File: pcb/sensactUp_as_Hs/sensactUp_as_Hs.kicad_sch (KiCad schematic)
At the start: 43 parts, among them J1 EXT_ROT, J2 SensactBusConnector, J3 24V+CAN IN, J4 24V+CAN OUT, J5 24V+CAN OUT, J6 24V+CAN OUT, J7 12V LED, Q1 AO3400A, Q2 AO3400A, Q3 AO3400A, SW1 EC11, SW2 RotaryEncoder, SW3 TERM OFF, U1 DS18B20, U2 ESP32-S3-DevKitC, U3 DCDC_MP2315, U4 DCDC_MP2315, U5 SN65HVD230, U6 PCA9685PW

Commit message: sensactUP_as_UP forgotten files
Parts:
- removed SW2: RotaryEncoder, symbol Device:RotaryEncoder
- added C6: u1, Capacitor_SMD:C_0805_2012Metric_Pad1.18x1.45mm_HandSolder, symbol Device:C
- added C7: 1u, Capacitor_SMD:C_0805_2012Metric_Pad1.18x1.45mm_HandSolder, symbol Device:C
- added J10, J11, J13, J14, J8, J9: OUT0-3, liebler_CONN:PhoenixContact_MCV_1,5_4-G-3.5_1x04_P3.50mm_Vertical_smallerCourtyard, symbol Connector_Generic:Conn_01x04
- added J12: OUT0-3, liebler_CONN:PhoenixContact_MC_1,5_4-G-3.5_1x04_P3.50mm_Horizontal_smallerCourtyard, symbol Connector_Generic:Conn_01x04
- added J15, J16, J17, J18, J19, J20, J21: Conn_01x04, Connector_PinHeader_2.54mm:PinHeader_1x04_P2.54mm_Vertical, symbol Connector_Generic:Conn_01x04
- added U7: PCA9555PW, liebler_SEMICONDUCTORS:TSSOP-24_4.4x7.8mm_Pitch0.65mm_handsolder, symbol Interface_Expansion:PCA9555PW
- J1: value EXT_ROT -> Conn_01x04; footprint Connector_Phoenix_MC:PhoenixContact_MCV_1,5_4-G-3.5_1x04_P3.50mm_Vertical -> Connector_PinHeader_2.54mm:PinHeader_1x04_P2.54mm_Vertical
- J5: value 24V+CAN OUT -> EXT_ENC
- J6: value 24V+CAN OUT -> OUT0-3
- R8, R9: value 10k -> 4k7
- U6: footprint Package_SO:TSSOP-28_4.4x9.7mm_P0.65mm -> liebler_SEMICONDUCTORS:TSSOP-28_4.4x9.7mm_Pitch0.65mm_handsolder
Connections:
- net PWM0 is gone; now on net L8: R11.1
- net PWM1 is gone; now on net L7: R13.1
- net PWM2 is gone; now on net L6: R15.1
- net +3V3: now also C6.1, C7.1, U7.24 (VDD)
- net A: no longer J1.1 (Pin_1)
- net B: no longer J1.3 (Pin_3)
- net GND: now also J1.4 (Pin_4), J5.4 (Pin_4), J6.4 (Pin_4), C6.2, C7.2, J10.4 (Pin_4), J11.4 (Pin_4), J12.4 (Pin_4), J13.4 (Pin_4), J14.4 (Pin_4), J15.4 (Pin_4), J16.4 (Pin_4), J17.4 (Pin_4), J18.4 (Pin_4), J19.4 (Pin_4), J20.4 (Pin_4), J21.4 (Pin_4), J8.4 (Pin_4), J9.4 (Pin_4), U7.12 (VSS), U7.2 (A1), U7.21 (A0), U7.3 (A2); no longer J1.2 (Pin_2)
- net Onewire: now also U2.35 (GPIO38)
- net PROG_IO0: now also J5.3 (Pin_3)
- net ROT_A: now also J5.1 (Pin_1)
- net ROT_B: now also J5.2 (Pin_2)
- net S: no longer J1.4 (Pin_4)
- net SCL: now also U2.41 (GPIO1/ADC1_CH0), U7.22 (SCL)
- net SDA: now also U2.40 (GPIO2/ADC1_CH1), U7.23 (SDA)
- net T2: now reaches J6.1 (Pin_1)
- net T2: now also J18.1 (Pin_1), U7.6 (IO0_2)
- net T1: now reaches J6.2 (Pin_2)
- net T1: now also J18.2 (Pin_2), U7.5 (IO0_1)
- net T0: now reaches J6.3 (Pin_3)
- net T0: now also J18.3 (Pin_3), U7.4 (IO0_0)
- net L4: now reaches U6.10 (LED4)
- net L4: now also J11.2 (Pin_2), J15.2 (Pin_2)
- net L5: now reaches U6.11 (LED5)
- net L5: now also J11.1 (Pin_1), J15.1 (Pin_1)
- net L6: now reaches U6.12 (LED6)
- net L7: now reaches U6.13 (LED7)
- net L8: now reaches U6.15 (LED8)
- net L9: now reaches U6.16 (LED9)
- net L9: now also J10.3 (Pin_3), J16.3 (Pin_3)
- net L10: now reaches U6.17 (LED10)
- net L10: now also J10.2 (Pin_2), J16.2 (Pin_2)
- net L11: now reaches U6.18 (LED11)
- net L11: now also J10.1 (Pin_1), J16.1 (Pin_1)
- net L12: now reaches U6.19 (LED12)
- net L12: now also J17.3 (Pin_3), J9.3 (Pin_3)
- net L13: now reaches U6.20 (LED13)
- net L13: now also J17.2 (Pin_2), J9.2 (Pin_2)
- net L14: now reaches U6.21 (LED14)
- net L14: now also J17.1 (Pin_1), J9.1 (Pin_1)
- net L15: now reaches U6.22 (LED15)
- net L0: now reaches U6.6 (LED0)
- net L0: now also J1.3 (Pin_3), J8.3 (Pin_3)
- net L1: now reaches U6.7 (LED1)
- net L1: now also J1.2 (Pin_2), J8.2 (Pin_2)
- net L2: now reaches U6.8 (LED2)
- net L2: now also J1.1 (Pin_1), J8.1 (Pin_1)
- net L3: now reaches U6.9 (LED3)
- net L3: now also J11.3 (Pin_3), J15.3 (Pin_3)
- new net T10: J14.2 (Pin_2), J21.2 (Pin_2), U7.15 (IO1_2)
- new net T11: J14.1 (Pin_1), J21.1 (Pin_1), U7.16 (IO1_3)
- new net T12: U7.17 (IO1_4)
- new net T13: U7.18 (IO1_5)
- new net T14: U7.19 (IO1_6)
- new net T3: J12.3 (Pin_3), J19.3 (Pin_3), U7.7 (IO0_3)
- new net T4: J12.2 (Pin_2), J19.2 (Pin_2), U7.8 (IO0_4)
- new net T5: J12.1 (Pin_1), J19.1 (Pin_1), U7.9 (IO0_5)
- new net T6: J13.3 (Pin_3), J20.3 (Pin_3), U7.10 (IO0_6)
- new net T7: J13.2 (Pin_2), J20.2 (Pin_2), U7.11 (IO0_7)
- new net T8: J13.1 (Pin_1), J20.1 (Pin_1), U7.13 (IO1_0)
- new net T9: J14.3 (Pin_3), J21.3 (Pin_3), U7.14 (IO1_1)
- no-connect marks 3 -> 4
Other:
- moved on the sheet: J5, J6

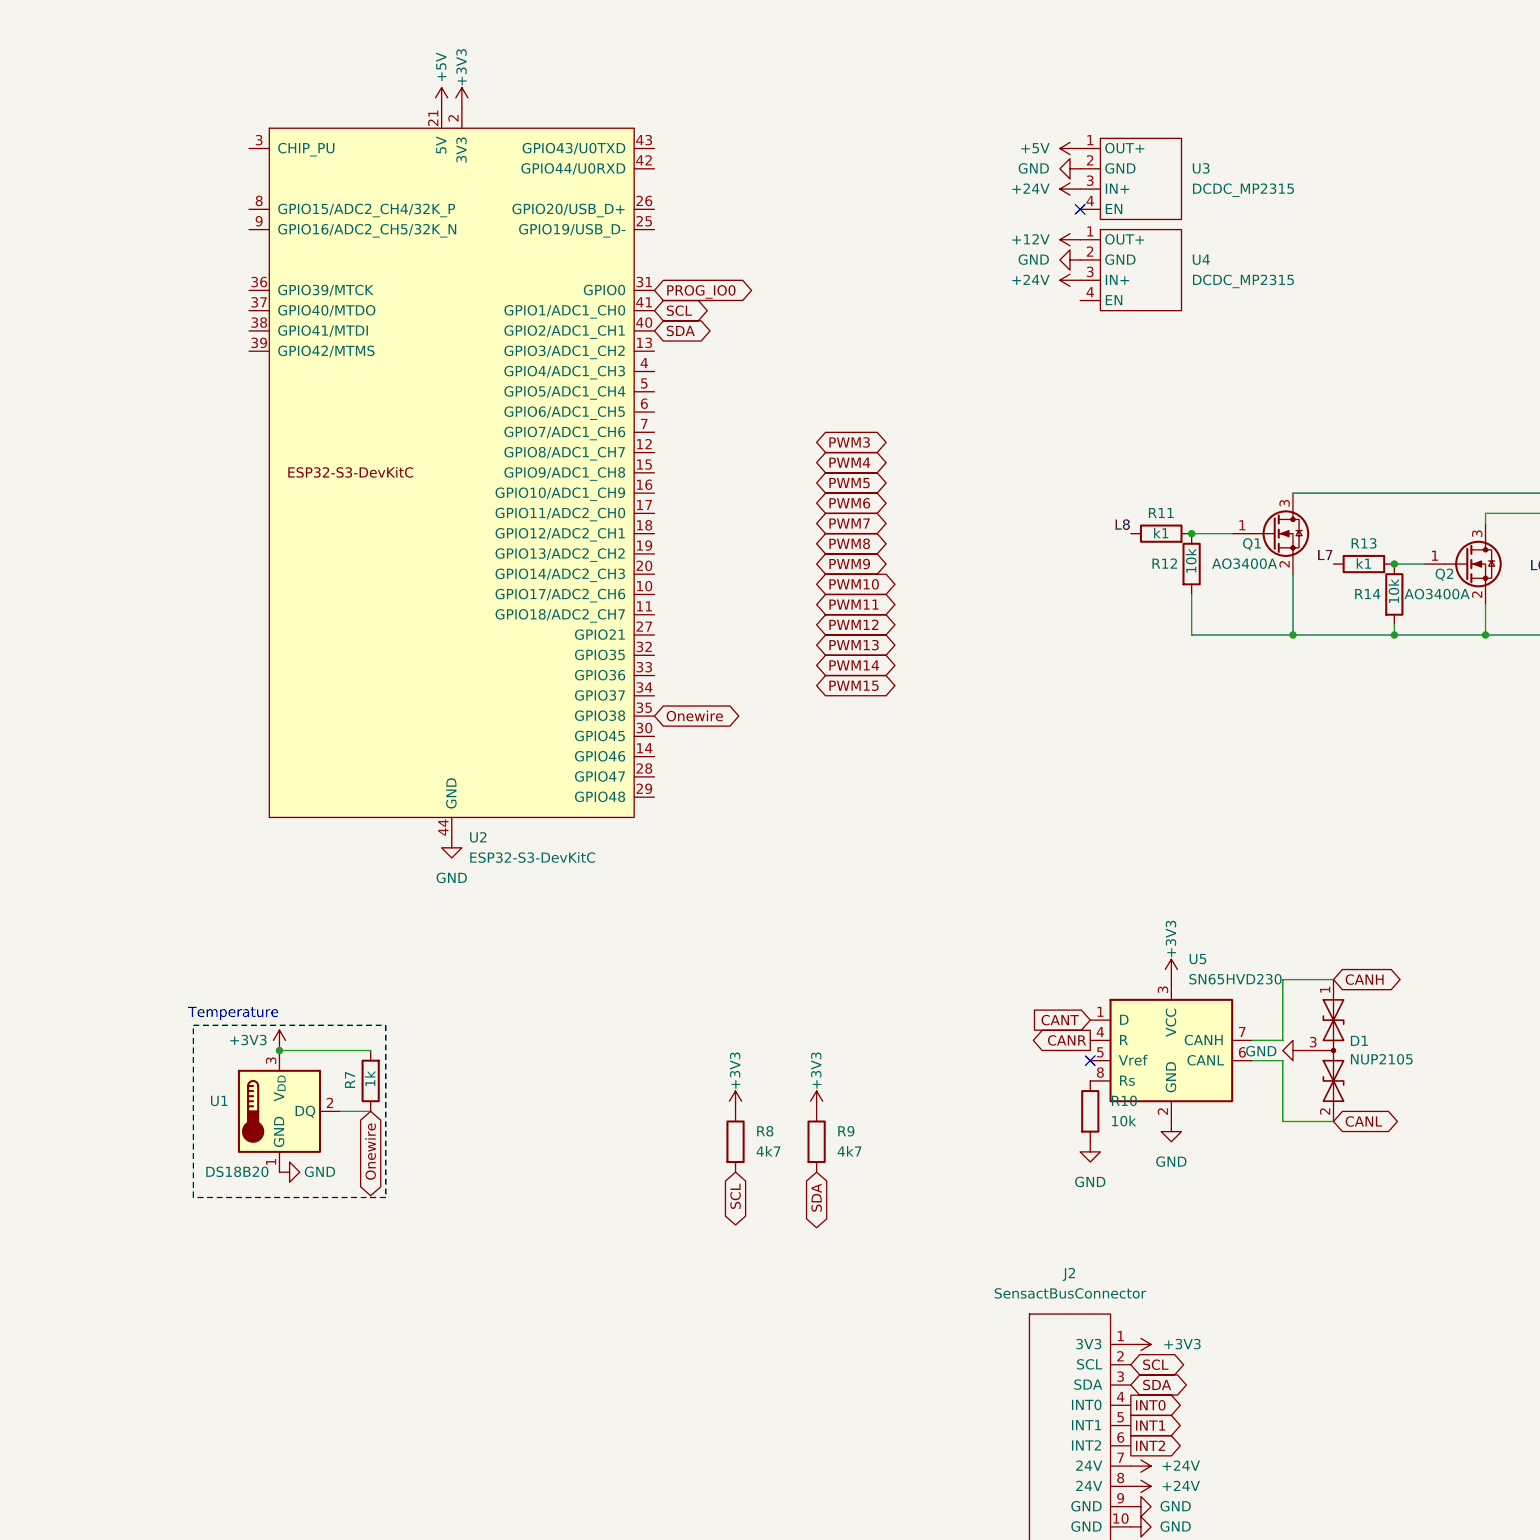
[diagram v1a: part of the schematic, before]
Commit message: Pin usage according to sensactRingEncoder
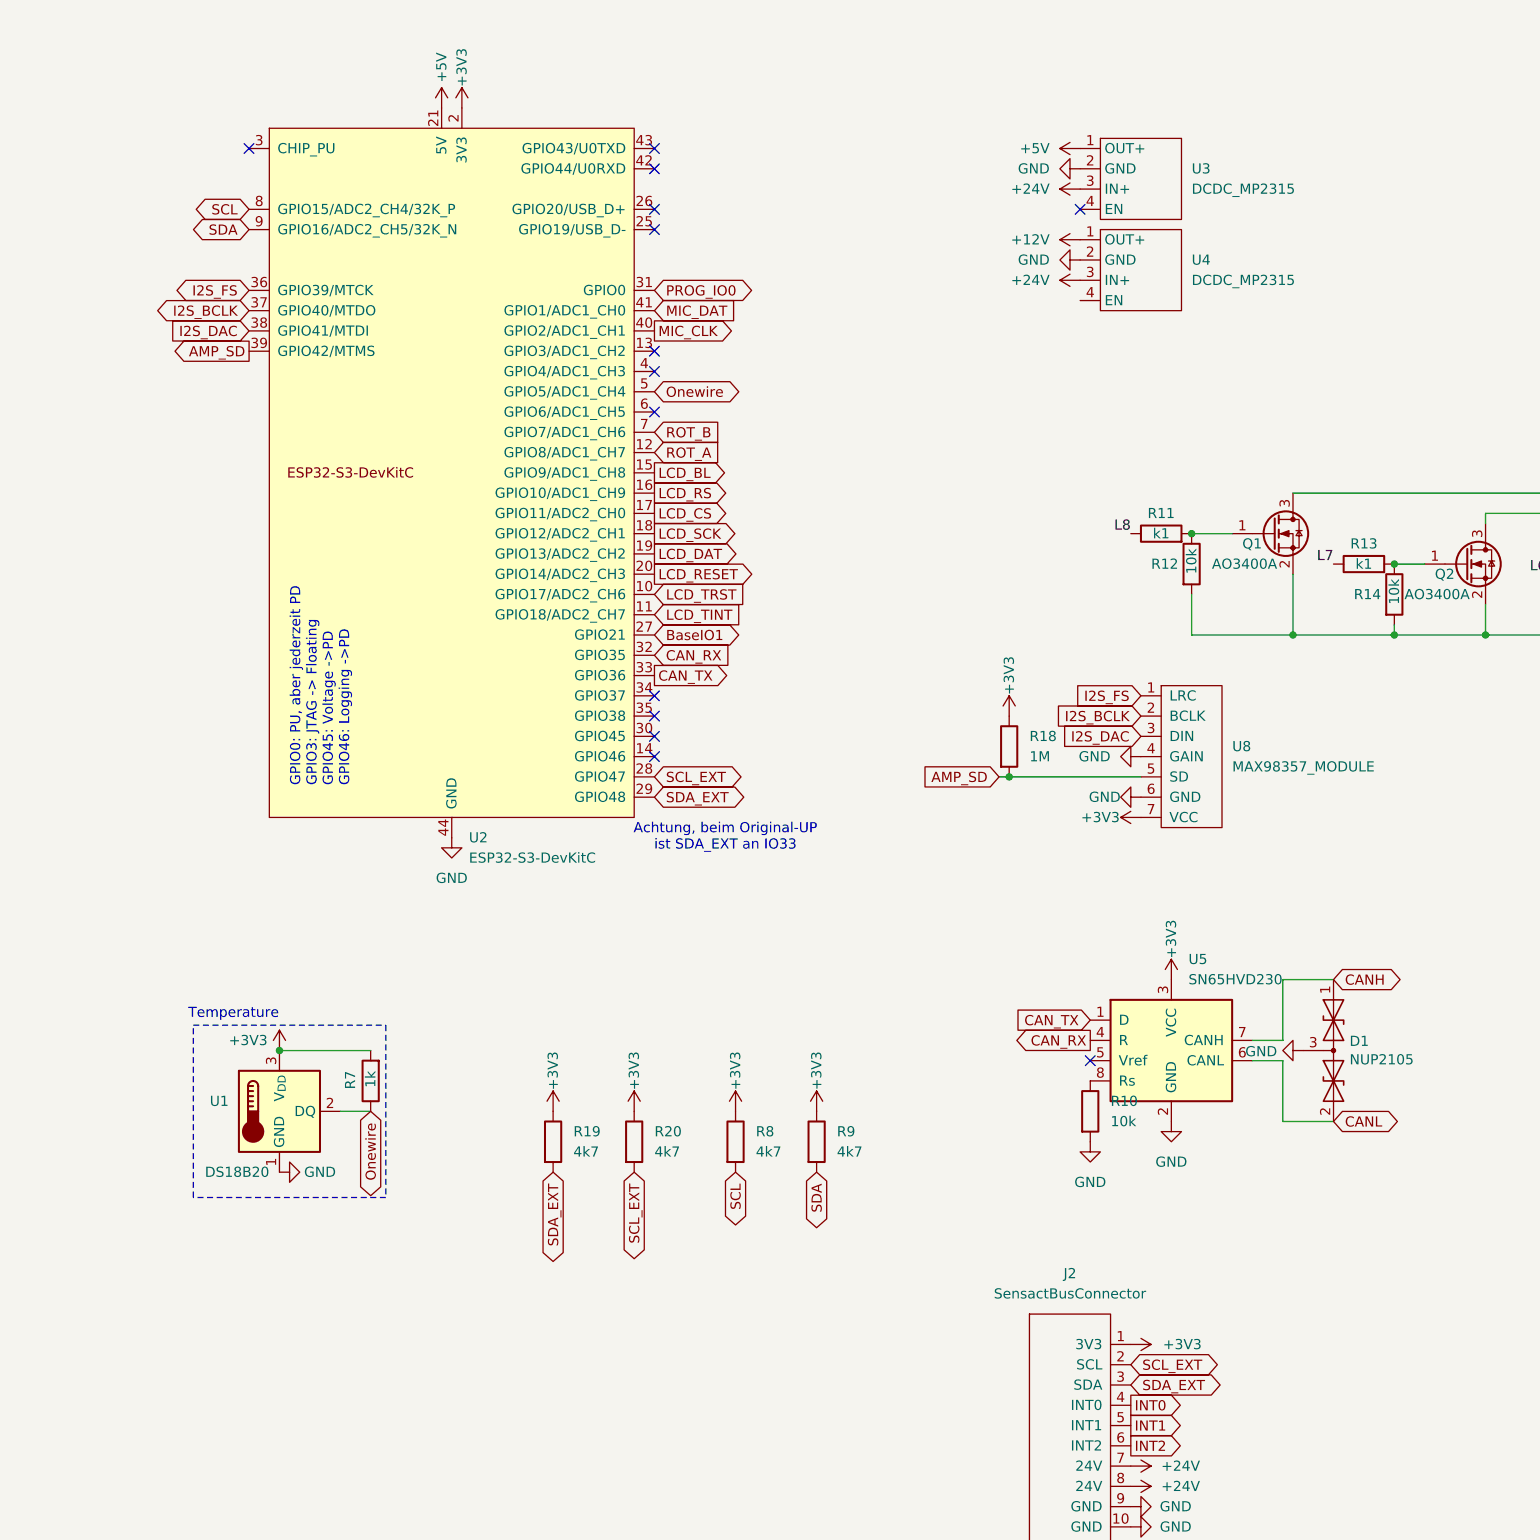
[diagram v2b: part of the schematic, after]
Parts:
- added R18: 1M, Resistor_SMD:R_0805_2012Metric_Pad1.20x1.40mm_HandSolder, symbol Device:R
- added R19, R20: 4k7, Resistor_SMD:R_0805_2012Metric_Pad1.20x1.40mm_HandSolder, symbol Device:R
- added U8: MAX98357_MODULE, Connector_PinHeader_2.54mm:PinHeader_1x07_P2.54mm_Vertical, symbol liebler_MODULES:MAX98357_MODULE
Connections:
- net CANR is gone; now on net CAN_RX: U5.4 (R)
- net CANT is gone; now on net CAN_TX: U5.1 (D)
- net +3V3: now also R18.1, R19.1, R20.1, U8.7 (VCC)
- net GND: now also U8.4 (GAIN), U8.6 (GND)
- net Onewire: now also U2.5 (GPIO5/ADC1_CH4); no longer U2.35 (GPIO38)
- net ROT_A: now also U2.12 (GPIO8/ADC1_CH7)
- net ROT_B: now also U2.7 (GPIO7/ADC1_CH6)
- net SCL: now also U2.8 (GPIO15/ADC2_CH4/32K_P); no longer J2.2 (SCL), U2.41 (GPIO1/ADC1_CH0)
- net SDA: now also U2.9 (GPIO16/ADC2_CH5/32K_N); no longer J2.3 (SDA), U2.40 (GPIO2/ADC1_CH1)
- net LCD_TRST: now reaches U2.10 (GPIO17/ADC2_CH6)
- net LCD_TINT: now reaches U2.11 (GPIO18/ADC2_CH7)
- net LCD_BL: now reaches U2.15 (GPIO9/ADC1_CH8)
- net LCD_RS: now reaches U2.16 (GPIO10/ADC1_CH9)
- net LCD_CS: now reaches U2.17 (GPIO11/ADC2_CH0)
- net LCD_SCK: now reaches U2.18 (GPIO12/ADC2_CH1)
- net LCD_DAT: now reaches U2.19 (GPIO13/ADC2_CH2)
- net LCD_RESET: now reaches U2.20 (GPIO14/ADC2_CH3)
- net BaseIO1: now reaches U2.27 (GPIO21)
- net SCL_EXT: now reaches U2.28 (GPIO47)
- net SCL_EXT: now also J2.2 (SCL), R20.2
- net SDA_EXT: now reaches U2.29 (GPIO48)
- net SDA_EXT: now also J2.3 (SDA), R19.2
- net CAN_RX: now reaches U2.32 (GPIO35)
- net CAN_TX: now reaches U2.33 (GPIO36)
- net I2S_FS: now reaches U2.36 (GPIO39/MTCK)
- net I2S_FS: now also U8.1 (LRC)
- net I2S_BCLK: now reaches U2.37 (GPIO40/MTDO)
- net I2S_BCLK: now also U8.2 (BCLK)
- net I2S_DAC: now reaches U2.38 (GPIO41/MTDI)
- net I2S_DAC: now also U8.3 (DIN)
- net AMP_SD: now reaches U2.39 (GPIO42/MTMS)
- net AMP_SD: now also R18.2, U8.5 (SD)
- new net MIC_CLK: U2.40 (GPIO2/ADC1_CH1)
- new net MIC_DAT: U2.41 (GPIO1/ADC1_CH0)
- no-connect marks 4 -> 16
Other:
- note added: "Achtung, beim Original-UP ist SDA_EXT an IO33"
- note added: "GPIO0: PU, aber jederzeit PD GPIO3: JTAG -> Floating GPIO45: Voltage ->PD GPIO46: Logging ->PD"

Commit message: sensactUp_as_Hs
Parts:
- removed C7: 1u, Capacitor_SMD:C_0805_2012Metric_Pad1.18x1.45mm_HandSolder, symbol Device:C
- removed J1, J15, J16, J17, J18, J19, J20, J21: Conn_01x04, Connector_PinHeader_2.54mm:PinHeader_1x04_P2.54mm_Vertical, symbol Connector_Generic:Conn_01x04
- removed J10, J11, J13, J14, J8, J9: OUT0-3, liebler_CONN:PhoenixContact_MCV_1,5_4-G-3.5_1x04_P3.50mm_Vertical_smallerCourtyard, symbol Connector_Generic:Conn_01x04
- removed J12, J6: OUT0-3, liebler_CONN:PhoenixContact_MC_1,5_4-G-3.5_1x04_P3.50mm_Horizontal_smallerCourtyard, symbol Connector_Generic:Conn_01x04
- removed J4: 24V+CAN OUT, liebler_CONN:PhoenixContact_MC_1,5_4-G-3.5_1x04_P3.50mm_Horizontal_smallerCourtyard, symbol Connector_Generic:Conn_01x04
- removed J5: EXT_ENC, liebler_CONN:PhoenixContact_MC_1,5_4-G-3.5_1x04_P3.50mm_Horizontal_smallerCourtyard, symbol Connector_Generic:Conn_01x04
- removed J7: 12V LED, liebler_CONN:PhoenixContact_MC_1,5_4-G-3.5_1x04_P3.50mm_Horizontal_smallerCourtyard, symbol Connector_Generic:Conn_01x04
- removed Q1, Q2, Q3: AO3400A, Package_TO_SOT_SMD:SOT-23_Handsoldering, symbol Transistor_FET:AO3400A
- removed SW1: EC11, liebler_MECH:RotaryEncoder_Alps_EC11E-Switch_Vertical_H20mm, symbol Device:RotaryEncoder_Switch_MP
- removed U6: PCA9685PW, liebler_SEMICONDUCTORS:TSSOP-28_4.4x9.7mm_Pitch0.65mm_handsolder, symbol Driver_LED:PCA9685PW
- removed U7: PCA9555PW, liebler_SEMICONDUCTORS:TSSOP-24_4.4x7.8mm_Pitch0.65mm_handsolder, symbol Interface_Expansion:PCA9555PW
- added C10, C11, C12: 10n, Capacitor_SMD:C_0805_2012Metric_Pad1.18x1.45mm_HandSolder, symbol Device:C
- added C8, C9: u1, Capacitor_SMD:C_0805_2012Metric_Pad1.18x1.45mm_HandSolder, symbol Device:C
- added J10: ROT1, liebler_CONN:PhoenixContact_MCV_1,5_5-G-3.81_1x05_P3.81mm_Vertical_smallerCourtyard, symbol Connector_Generic:Conn_01x05
- added J11: OneWire, liebler_CONN:PhoenixContact_MCV_1,5_5-G-3.81_1x05_P3.81mm_Vertical_smallerCourtyard, symbol Connector_Generic:Conn_01x05
- added J12: LED Driver, Connector_PinHeader_2.54mm:PinHeader_1x08_P2.54mm_Vertical, symbol Connector_Generic:Conn_01x08
- added J4, J7, J8, J9: LED, liebler_CONN:PhoenixContact_MCV_1,5_5-G-3.81_1x05_P3.81mm_Vertical_smallerCourtyard, symbol Connector_Generic:Conn_01x05
- added J5: ROT2, liebler_CONN:PhoenixContact_MCV_1,5_5-G-3.81_1x05_P3.81mm_Vertical_smallerCourtyard, symbol Connector_Generic:Conn_01x05
- added J6: LED Driver, liebler_CONN:PhoenixContact_MC_0,5_8-G-2.5_1x08_P2.50mm_Horizontal, symbol Connector_Generic:Conn_01x08
- added U10, U9: TPL7407LAPW, Package_SO:TSSOP-16_4.4x5mm_P0.65mm, symbol Transistor_Array:TPL7407LAPW
- added U11: DS2482, liebler_SEMICONDUCTORS:SOIC-8_3.9x4.9mm_P1.27mm_handsolder, symbol liebler_SEMICONDUCTORS:DS2482
- added U7: PCA9685PW, liebler_SEMICONDUCTORS:TSSOP-28_4.4x9.7mm_Pitch0.65mm_handsolder, symbol Driver_LED:PCA9685PW
- J3: footprint liebler_CONN:PhoenixContact_MC_1,5_4-G-3.5_1x04_P3.50mm_Horizontal_smallerCourtyard -> liebler_CONN:PhoenixContact_MCV_1,5_4-G-3.5_1x04_P3.50mm_Vertical_smallerCourtyard
- R11, R13, R15: value k1 -> 10k
- U2: footprint Espressif:ESP32-S3-DevKitC -> liebler_MODULES:ESP32-S3 chinese dev board
- U3, U4: footprint liebler_MODULES:DCDC_MP2315 -> liebler_MODULES:DCDC_MP2315_horizontal
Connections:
- net BaseIO1 is gone; now on net INT1: U2.27 (GPIO21)
- net L7 is gone; now on net ROT1_S: R13.1
- net LCD_BL is gone; now on net INT0: U2.15 (GPIO9/ADC1_CH8)
- net LCD_CS is gone; now on net CAN_RX: U2.17 (GPIO11/ADC2_CH0)
- net LCD_DAT is gone; now on net SDA_EXT: U2.19 (GPIO13/ADC2_CH2)
- net LCD_RESET is gone; now on net SCL_EXT: U2.20 (GPIO14/ADC2_CH3)
- net LCD_RS is gone; now on net INT2: U2.16 (GPIO10/ADC1_CH9)
- net LCD_SCK is gone; now on net CAN_TX: U2.18 (GPIO12/ADC2_CH1)
- net LCD_TINT is gone; now on net L2: U2.11 (GPIO18/ADC2_CH7)
- net LCD_TRST is gone; now on net L1: U2.10 (GPIO17/ADC2_CH6)
- net MIC_DAT is gone; now on net +3V3: U2.41 (GPIO1/ADC1_CH0)
- net +12V: now also C8.1, C9.1, J11.2 (Pin_2), J4.5 (Pin_5), J7.5 (Pin_5), J8.5 (Pin_5), J9.5 (Pin_5), U10.9 (COM), U9.9 (COM)
- net +24V: now also J3.4 (Pin_4), J11.1 (Pin_1); no longer J3.1 (Pin_1)
- net +3V3: now also R12.1, R14.1, R16.1, R6.1, J11.3 (Pin_3), U11.1 (VCC), U7.1 (A0), U7.28 (VDD); no longer R5.1
- net CANH: now also SW3.1 (A)
- net CANL: now also J3.2 (Pin_2); no longer J3.4 (Pin_4)
- net CAN_RX: no longer U2.32 (GPIO35)
- net CAN_TX: no longer U2.33 (GPIO36)
- net GND: now also C3.1, J3.1 (Pin_1), C10.1, C11.1, C12.1, C8.2, C9.2, J10.1 (Pin_1), J10.2 (Pin_2), J11.5 (Pin_5), J12.7 (Pin_7), J12.8 (Pin_8), J5.1 (Pin_1), J5.2 (Pin_2), J6.7 (Pin_7), J6.8 (Pin_8), U10.8 (GND), U11.3 (GND), U11.7 (AD1), U11.8 (AD0), U7.14 (VSS), U7.2 (A1), U7.23 (~{OE}), U7.24 (A5), U7.3 (A2), U7.4 (A3), U7.5 (A4), U9.8 (GND); no longer C3.2, J3.2 (Pin_2), R12.2, R14.2, R16.2
- net L0: now also U2.32 (GPIO35), J12.6 (Pin_6), J6.6 (Pin_6)
- net L1: now also J12.5 (Pin_5), J6.5 (Pin_5)
- net L2: now also J12.4 (Pin_4), J6.4 (Pin_4)
- net L3: now also U2.29 (GPIO48), J12.3 (Pin_3), J6.3 (Pin_3)
- net L4: now also U2.12 (GPIO8/ADC1_CH7), J12.2 (Pin_2), J6.2 (Pin_2)
- net L5: now also U2.28 (GPIO47), J12.1 (Pin_1), J6.1 (Pin_1)
- net Onewire: now also U2.13 (GPIO3/ADC1_CH2); no longer U2.5 (GPIO5/ADC1_CH4)
- net SCL: now also U2.34 (GPIO37), U11.4 (SCL), U7.26 (SCL); no longer U2.8 (GPIO15/ADC2_CH4/32K_P)
- net SCL_EXT: no longer U2.28 (GPIO47)
- net SDA: now also U2.35 (GPIO38), U11.5 (SDA), U7.27 (SDA); no longer U2.9 (GPIO16/ADC2_CH5/32K_N)
- net SDA_EXT: no longer U2.29 (GPIO48)
- net ROT1_SS: now reaches R13.2
- net ROT1_SS: now also R14.2, J10.3 (Pin_3); no longer R14.1
- net ROT2_BB: now reaches R11.2
- net ROT2_BB: now also R12.2, J5.4 (Pin_4); no longer R12.1
- net ROT2_SS: now reaches R15.2
- net ROT2_SS: now also R16.2, J5.3 (Pin_3); no longer R16.1
- net ROT1_S: now reaches U2.4 (GPIO4/ADC1_CH3)
- net ROT1_S: now also C11.2
- net ROT1_A: now reaches U2.6 (GPIO6/ADC1_CH5)
- net ROT1_A: now also C2.2, R2.1
- net A renamed ROT1_AA
- net ROT1_AA: now also R2.2, J10.5 (Pin_5); no longer R1.2
- net B renamed ROT2_AA
- net ROT2_AA: now also R1.2, J5.5 (Pin_5); no longer R2.2
- net L6 renamed ROT2_S
- net ROT2_S: now also U2.7 (GPIO7/ADC1_CH6), C12.2
- net L8 renamed ROT2_B
- net ROT2_B: now also U2.8 (GPIO15/ADC2_CH4/32K_P), C10.2
- net MIC_CLK: no longer names the net of U2.40 (GPIO2/ADC1_CH1)
- removed net PROG_IO0: C3.1, R6.1, U2.31 (GPIO0)
- net ROT_A renamed ROT2_A
- net ROT2_A: now also U2.9 (GPIO16/ADC2_CH5/32K_N); no longer U2.12 (GPIO8/ADC1_CH7)
- removed net ROT_B: C2.2, R2.1, U2.7 (GPIO7/ADC1_CH6)
- net S renamed ROT1_BB
- net ROT1_BB: now also J10.4 (Pin_4)
- new net: J11.4 (Pin_4), U11.2 (IO)
- new net LED0: J9.4 (Pin_4), U9.10 (OUT7)
- new net LED1: J9.3 (Pin_3), U9.11 (OUT6)
- new net LED10: J4.2 (Pin_2), U10.13 (OUT4)
- new net LED11: J4.1 (Pin_1), U10.14 (OUT3)
- new net LED12: J8.1 (Pin_1), U10.15 (OUT2)
- new net LED13: J8.2 (Pin_2), U10.16 (OUT1)
- new net LED2: J9.2 (Pin_2), U9.12 (OUT5)
- new net LED3: J9.1 (Pin_1), U9.13 (OUT4)
- new net LED4: J7.4 (Pin_4), U9.14 (OUT3)
- new net LED5: J7.3 (Pin_3), U9.15 (OUT2)
- new net LED6: J7.2 (Pin_2), U9.16 (OUT1)
- new net LED7: J7.1 (Pin_1), U10.10 (OUT7)
- new net LED8: J4.4 (Pin_4), U10.11 (OUT6)
- new net LED9: J4.3 (Pin_3), U10.12 (OUT5)
- new net LED_G_0: U7.6 (LED0), U9.7 (IN7)
- new net LED_G_1: U7.7 (LED1), U9.6 (IN6)
- new net LED_G_10: U10.4 (IN4), U7.17 (LED10)
- new net LED_G_11: U10.3 (IN3), U7.18 (LED11)
- new net LED_G_12: U10.2 (IN2), U7.19 (LED12)
- new net LED_G_13: U10.1 (IN1), U7.20 (LED13)
- new net LED_G_14: J8.3 (Pin_3), U7.21 (LED14)
- new net LED_G_15: J8.4 (Pin_4), U7.22 (LED15)
- new net LED_G_2: U7.8 (LED2), U9.5 (IN5)
- new net LED_G_3: U7.9 (LED3), U9.4 (IN4)
- new net LED_G_4: U7.10 (LED4), U9.3 (IN3)
- new net LED_G_5: U7.11 (LED5), U9.2 (IN2)
- new net LED_G_6: U7.12 (LED6), U9.1 (IN1)
- new net LED_G_7: U10.7 (IN7), U7.13 (LED7)
- new net LED_G_8: U10.6 (IN6), U7.15 (LED8)
- new net LED_G_9: U10.5 (IN5), U7.16 (LED9)
- new net ROT1_B: C3.2, R5.1, U2.5 (GPIO5/ADC1_CH4)
- no-connect marks 16 -> 14
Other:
- note removed: "Achtung, beim Original-UP ist SDA_EXT an IO33"
- moved on the sheet: C2, C5, R2, R3
